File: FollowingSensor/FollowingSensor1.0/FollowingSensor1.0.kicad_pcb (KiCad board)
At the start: 2 copper layers, 101.6 x 33.9 mm, 40 parts, among them J1 Conn_01x18, Q1 TEMT7100X01, Q10 TEMT7100X01, Q11 TEMT7100X01, Q12 TEMT7100X01, Q13 TEMT7100X01, Q14 TEMT7100X01, Q2 TEMT7100X01, Q3 TEMT7100X01, Q4 TEMT7100X01, Q5 TEMT7100X01, Q6 TEMT7100X01, Q7 TEMT7100X01, Q8 TEMT7100X01, Q9 TEMT7100X01

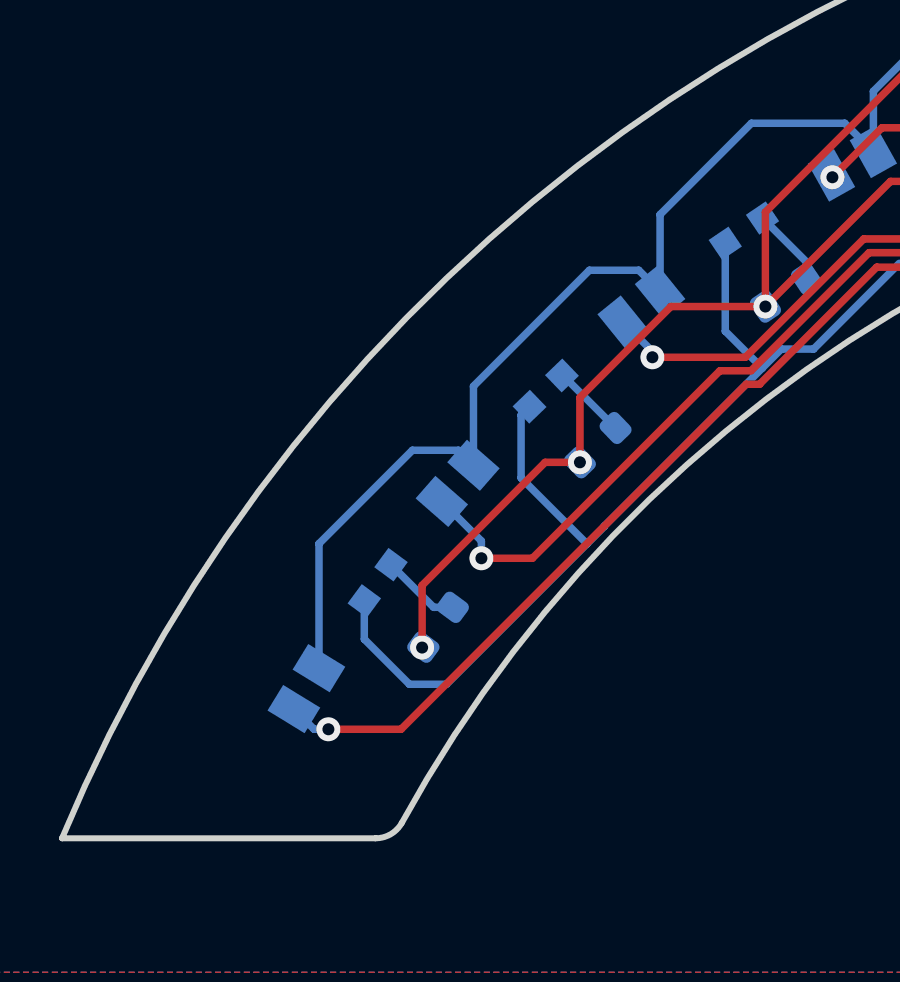
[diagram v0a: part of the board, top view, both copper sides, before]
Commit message: add logo
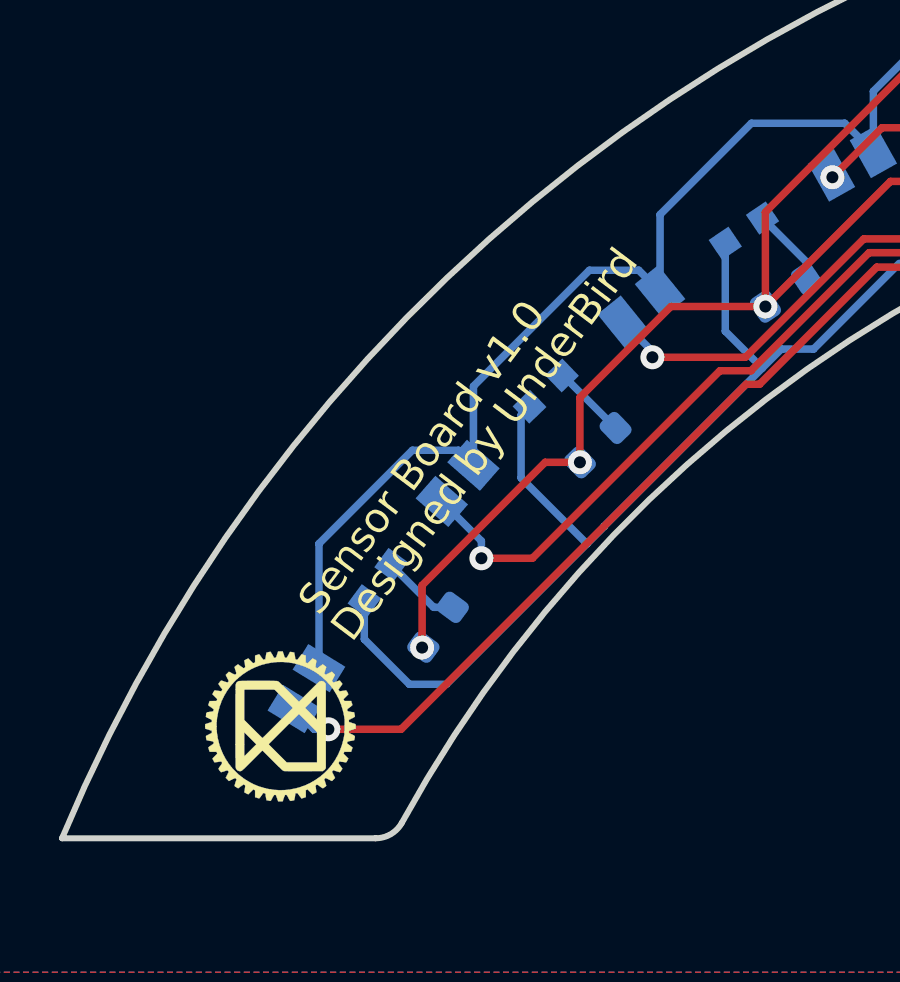
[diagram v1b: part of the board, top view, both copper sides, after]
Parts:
- added G***: LOGO, Symbol:SH-Logo_5x5mm, F.Cu at (106.5, 96.8)
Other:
- board text added: "Designed by UnderBird"
- board text added: "Sensor Board v1.0"

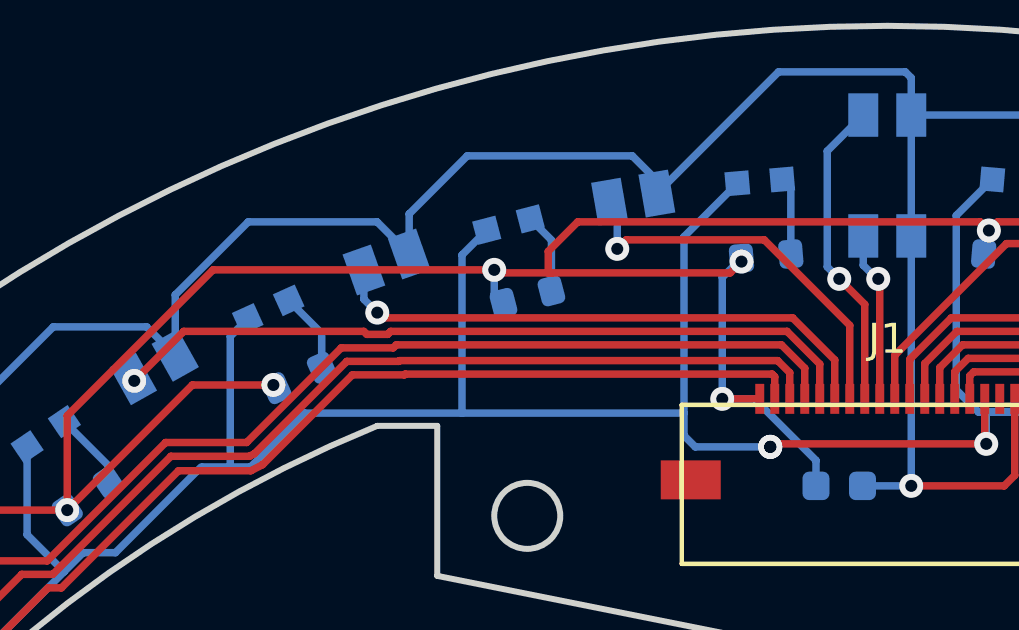
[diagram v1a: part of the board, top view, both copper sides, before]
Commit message: remove antena and move referencse by main board
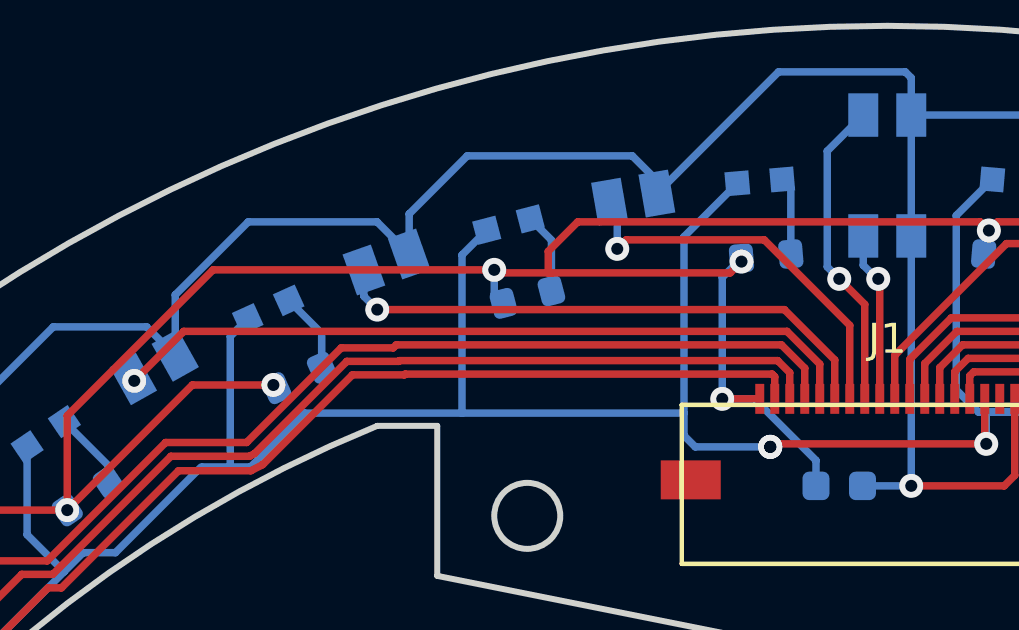
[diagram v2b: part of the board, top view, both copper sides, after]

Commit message: moved reference
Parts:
- moved G*** 0.76 mm to (105.8, 96.5), turned to 53 degrees
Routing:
- net GND: vias 1 -> 6
